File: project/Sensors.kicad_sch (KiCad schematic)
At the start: 21 parts, among them IC201 APDS-9306-065, IC202 BMI270, IC203 BMP581, IC204 LIS2MDLTR, IC205 BME688, Q201 DMG1013UW-7

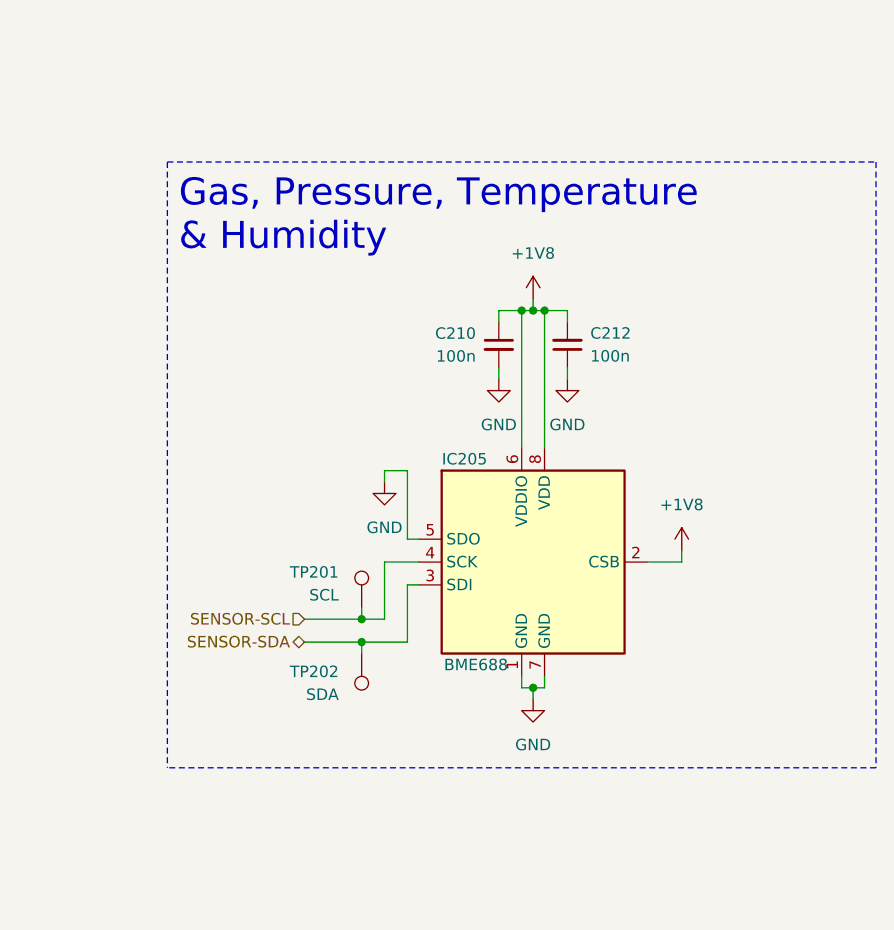
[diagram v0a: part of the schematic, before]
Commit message: PCB: Remove BME688 and USB switch
- Implement #106
- Remove USB switch and the required components

Signed-off-by: Daniel Kampert <danielkampert@kampis-elektroecke.de>
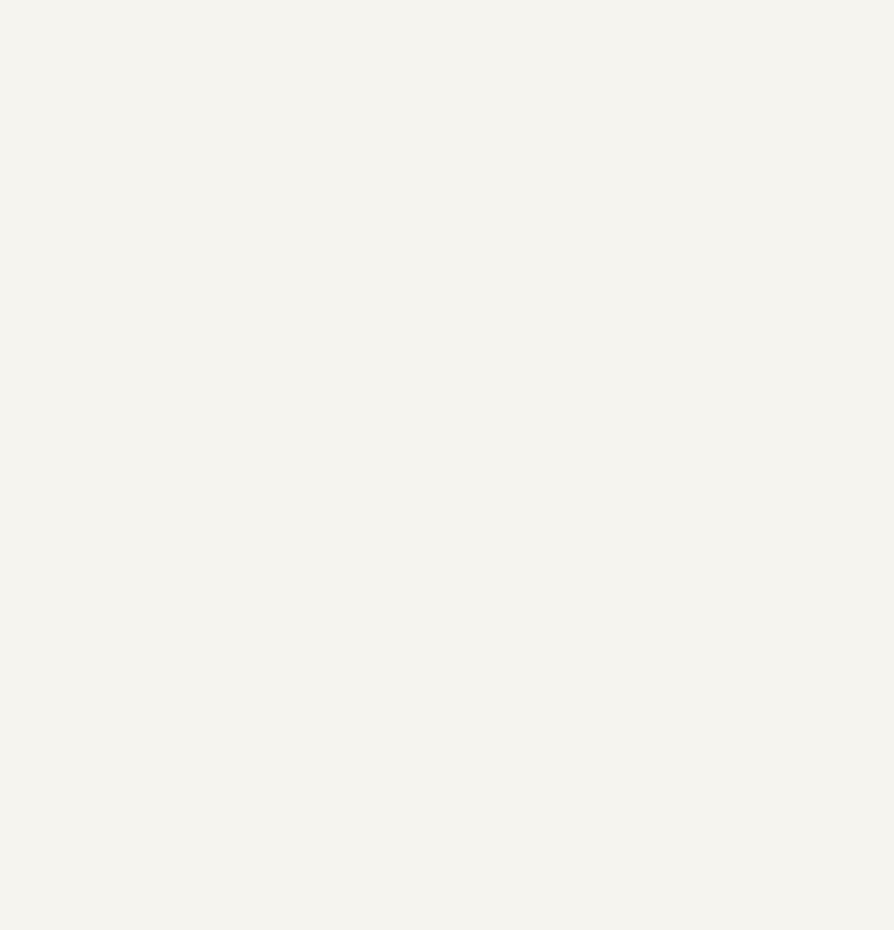
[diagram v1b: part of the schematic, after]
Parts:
- removed C210, C212: 100n, Capacitor_SMD:C_0603_1608Metric, symbol Device:C_Small
- removed IC205: BME688, Package_LGA_Kampi:Bosch_LGA-8_3x3mm_P0.8mm_ClockwisePinNumbering, symbol Bosch_Kampi:BME688
- removed TP201: SCL, TestPoint:TestPoint_Pad_D1.0mm, symbol Connector:TestPoint
- removed TP202: SDA, TestPoint:TestPoint_Pad_D1.0mm, symbol Connector:TestPoint
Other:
- note removed: "Gas, Pressure, Temperature & Humidity"
- title: ZSWatch v2 -> ZSWatch v3
